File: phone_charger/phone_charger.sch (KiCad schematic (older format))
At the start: 8 parts

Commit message: added in precision enable for phone charger
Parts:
- added R?: 56k (1%), symbol device:R
- added R?: 10.2k (1%), symbol device:R
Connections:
- net labels removed: reg_en
- wire segments 19 -> 24
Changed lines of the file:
@@
 EESchema Schematic File Version 4
+LIBS:phone_charger-cache
 EELAYER 26 0
 EELAYER END
@@
 L device:C C?
 U 1 1 5B8626AF
-P 7500 1500
-F 0 "C?" H 7615 1546 50  0000 L CNN
-F 1 "10u (25V)" H 7615 1455 50  0000 L CNN
-F 2 "" H 7538 1350 50  0001 C CNN
-F 3 "" H 7500 1500 50  0001 C CNN
-	1    7500 1500
+P 7100 1500
+F 0 "C?" H 7215 1546 50  0000 L CNN
+F 1 "10u (25V)" H 7215 1455 50  0000 L CNN
+F 2 "" H 7138 1350 50  0001 C CNN
+F 3 "" H 7100 1500 50  0001 C CNN
+	1    7100 1500
 	1    0    0    -1
 $EndComp
@@
 L power:GND #PWR?
 U 1 1 5B862781
-P 7500 1800
-F 0 "#PWR?" H 7500 1550 50  0001 C CNN
-F 1 "GND" H 7505 1627 50  0000 C CNN
-F 2 "" H 7500 1800 50  0001 C CNN
-F 3 "" H 7500 1800 50  0001 C CNN
-	1    7500 1800
-	1    0    0    -1
-$EndComp
-Wire Wire Line
-	7500 1650 7500 1800
-Wire Wire Line
-	7500 1350 7200 1350
+P 7100 1800
+F 0 "#PWR?" H 7100 1550 50  0001 C CNN
+F 1 "GND" H 7105 1627 50  0000 C CNN
+F 2 "" H 7100 1800 50  0001 C CNN
+F 3 "" H 7100 1800 50  0001 C CNN
+	1    7100 1800
+	1    0    0    -1
+$EndComp
+Wire Wire Line
+	7100 1650 7100 1800
+Wire Wire Line
+	7100 1350 6800 1350
 Wire Wire Line
 	9250 1250 9400 1250
-Text Label 7200 1350 0    50   ~ 0
+Text Label 6800 1350 0    50   ~ 0
 reg_in
 Text Label 10600 1600 0    50   ~ 0
@@
 Wire Wire Line
 	10500 1600 10900 1600
-Wire Wire Line
-	7500 1350 7950 1350
-Connection ~ 7500 1350
-Wire Wire Line
-	7950 1850 7700 1850
-Text Label 7700 1850 0    50   ~ 0
-reg_en
+Connection ~ 7100 1350
 Wire Wire Line
 	10100 1700 10100 1600
@@
 Wire Notes Line
 	6300 500  6300 3350
+$Comp
+L device:R R?
+U 1 1 5B863BCD
+P 7750 1600
+F 0 "R?" H 7820 1646 50  0000 L CNN
+F 1 "56k (1%)" H 7820 1555 50  0000 L CNN
+F 2 "" V 7680 1600 50  0001 C CNN
+F 3 "" H 7750 1600 50  0001 C CNN
+	1    7750 1600
+	1    0    0    -1
+$EndComp
+$Comp
+L device:R R?
+U 1 1 5B863BFA
+P 7750 2100
+F 0 "R?" H 7820 2146 50  0000 L CNN
+F 1 "10.2k (1%)" H 7820 2055 50  0000 L CNN
+F 2 "" V 7680 2100 50  0001 C CNN
+F 3 "" H 7750 2100 50  0001 C CNN
+	1    7750 2100
+	1    0    0    -1
+$EndComp
+$Comp
+L power:GND #PWR?
+U 1 1 5B863C22
+P 7750 2350
+F 0 "#PWR?" H 7750 2100 50  0001 C CNN
+F 1 "GND" H 7755 2177 50  0000 C CNN
+F 2 "" H 7750 2350 50  0001 C CNN
+F 3 "" H 7750 2350 50  0001 C CNN
+	1    7750 2350
+	1    0    0    -1
+$EndComp
+Wire Wire Line
+	7100 1350 7750 1350
+Wire Wire Line
+	7750 1350 7750 1450
+Connection ~ 7750 1350
+Wire Wire Line
+	7750 1350 7950 1350
+Wire Wire Line
+	7750 1750 7750 1850
+Wire Wire Line
+	7750 2250 7750 2350
+Wire Wire Line
+	7750 1850 7950 1850
+Connection ~ 7750 1850
+Wire Wire Line
+	7750 1850 7750 1950
 $EndSCHEMATC

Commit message: Rescue symbols
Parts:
- C? (x3): symbol device:C -> phone_charger-rescue:C-device
- D?: symbol device:D_Schottky -> phone_charger-rescue:D_Schottky-device
- L?: symbol device:L -> phone_charger-rescue:L-device
- R? (x4): symbol device:R -> phone_charger-rescue:R-device
- U?: symbol ADP2301:ADP2301AUJZ-R2 -> phone_charger-rescue:ADP2301AUJZ-R2-ADP2301
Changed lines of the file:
@@
 $EndDescr
 $Comp
-L ADP2301:ADP2301AUJZ-R2 U?
+L phone_charger-rescue:ADP2301AUJZ-R2-ADP2301 U?
 U 1 1 5B85ED45
 P 8600 1600
@@
 $EndComp
 $Comp
-L device:L L?
+L phone_charger-rescue:L-device L?
 U 1 1 5B85F10E
 P 9750 1600
@@
 $EndComp
 $Comp
-L device:C C?
+L phone_charger-rescue:C-device C?
 U 1 1 5B85F280
 P 10500 1850
@@
 $EndComp
 $Comp
-L device:R R?
+L phone_charger-rescue:R-device R?
 U 1 1 5B85F3D3
 P 10100 1850
@@
 $EndComp
 $Comp
-L device:R R?
+L phone_charger-rescue:R-device R?
 U 1 1 5B85F4C9
 P 10100 2300
@@
 $EndComp
 $Comp
-L device:D_Schottky D?
+L phone_charger-rescue:D_Schottky-device D?
 U 1 1 5B861A87
 P 9400 1750
@@
 $EndComp
 $Comp
-L device:C C?
+L phone_charger-rescue:C-device C?
 U 1 1 5B86257D
 P 9400 1400
@@
 $EndComp
 $Comp
-L device:C C?
+L phone_charger-rescue:C-device C?
 U 1 1 5B8626AF
 P 7100 1500
@@
 	6300 500  6300 3350
 $Comp
-L device:R R?
+L phone_charger-rescue:R-device R?
 U 1 1 5B863BCD
 P 7750 1600
@@
 $EndComp
 $Comp
-L device:R R?
+L phone_charger-rescue:R-device R?
 U 1 1 5B863BFA
 P 7750 2100

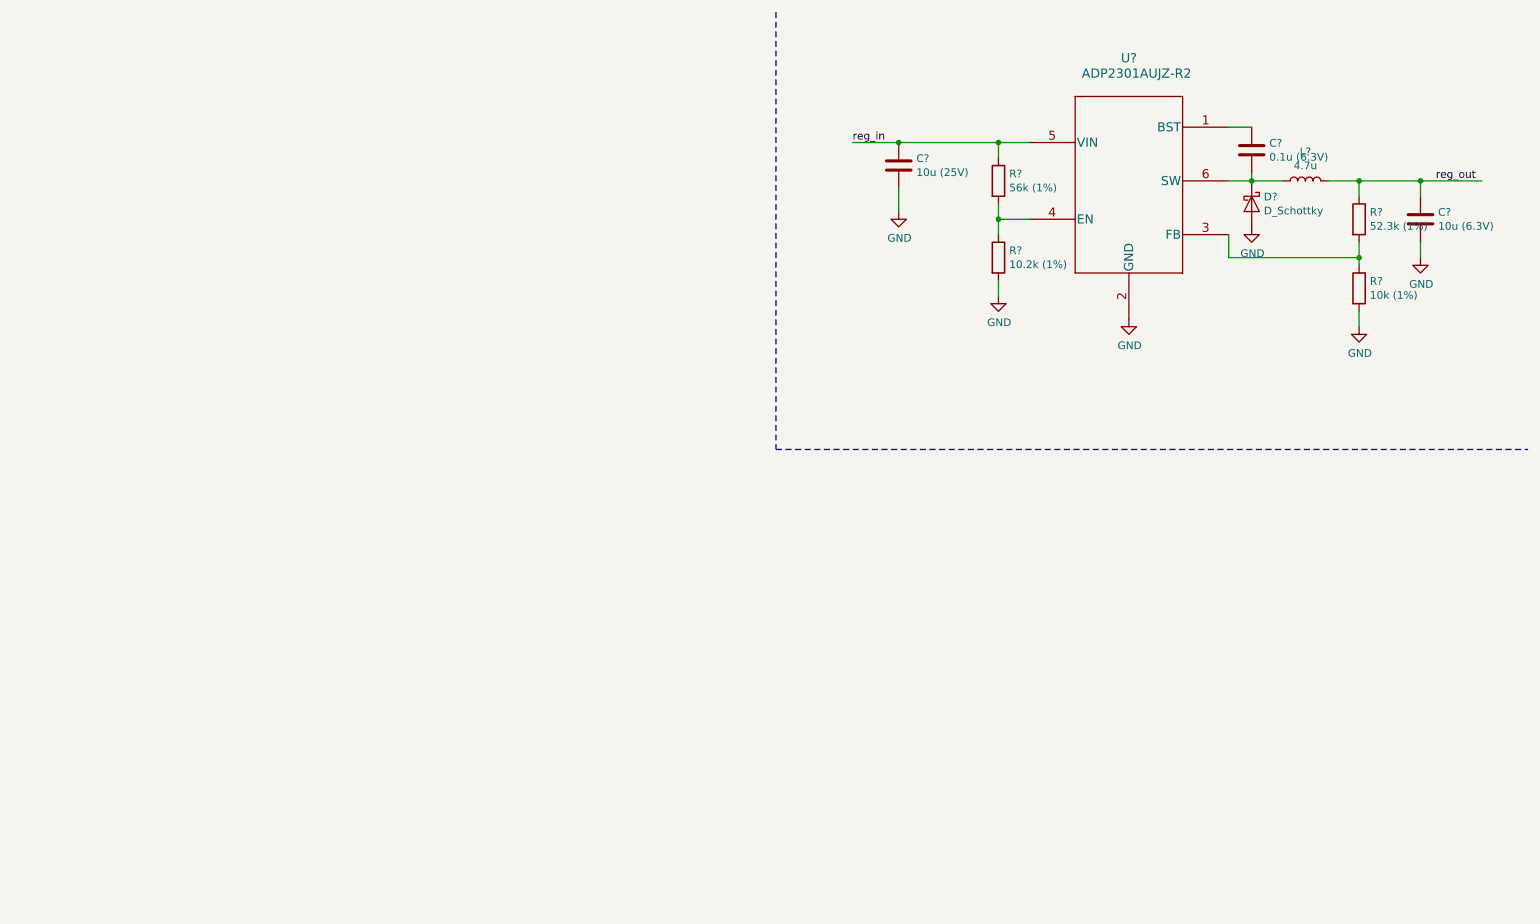
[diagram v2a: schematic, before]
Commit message: Add some top-level details
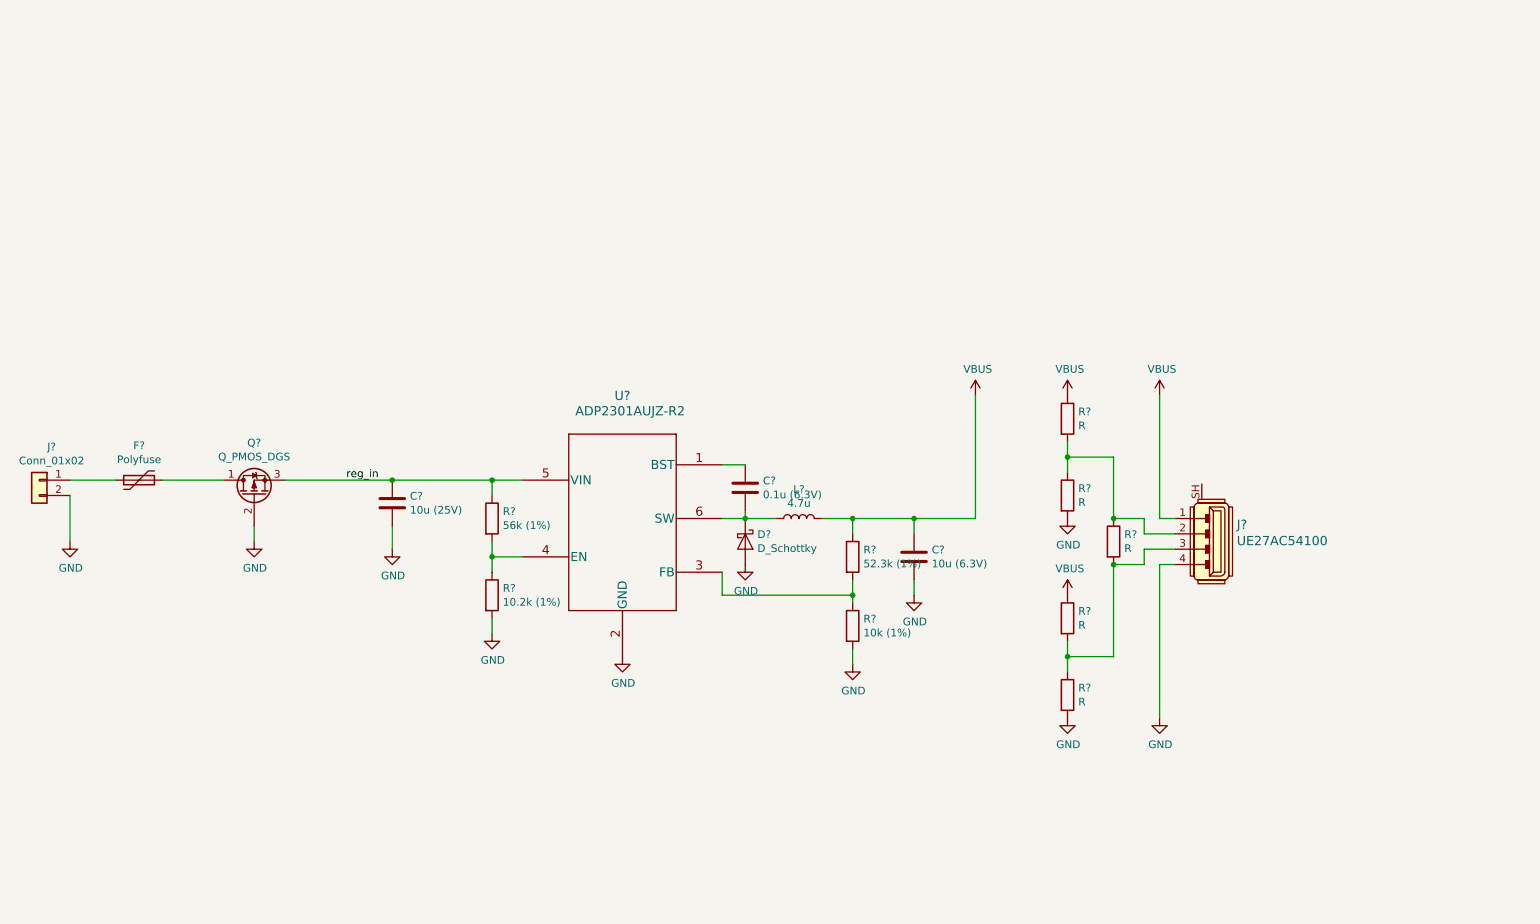
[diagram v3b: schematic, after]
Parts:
- added F?: Polyfuse, symbol Device:Polyfuse
- added J?: UE27AC54100, digikey-footprints:USB_A_Female_UE27AC54100, symbol dk_USB-DVI-HDMI-Connectors:UE27AC54100
- added J?: Conn_01x02, symbol Connector_Generic:Conn_01x02
- added Q?: Q_PMOS_DGS, symbol Device:Q_PMOS_DGS
- added R? (x5): R, symbol Device:R
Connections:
- net labels added: VBUS
- net labels removed: reg_out
- wire segments 24 -> 47
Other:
- moved on the sheet: C?, D?, L?, R?, U?

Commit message: Add values
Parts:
- R?: value R -> 75k
- R? (x2): value R -> 50k
- R?: value R -> 43k
- R?: value R -> 200
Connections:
- net D-: now reaches J?.2, R?.1, R?.1, R?.2
- net D+: now reaches J?.3, R?.1, R?.2, R?.2
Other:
- note added: "Populate EITHER Apple divider resistors or 200 ohm short."
- moved on the sheet: J?
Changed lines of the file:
@@
 L dk_USB-DVI-HDMI-Connectors:UE27AC54100 J?
 U 1 1 5B88DA27
-P 9200 3900
-F 0 "J?" H 9097 3840 60  0000 R CNN
-F 1 "UE27AC54100" H 9097 3946 60  0000 R CNN
-F 2 "digikey-footprints:USB_A_Female_UE27AC54100" H 9400 4100 60  0001 L CNN
-F 3 "https://www.amphenolcanada.com/ProductSearch/drawings/AC/UE27ACX4X0X.pdf" H 9400 4200 60  0001 L CNN
-F 4 "UE27AC54100-ND" H 9400 4300 60  0001 L CNN "Digi-Key_PN"
-F 5 "UE27AC54100" H 9400 4400 60  0001 L CNN "MPN"
-F 6 "Connectors, Interconnects" H 9400 4500 60  0001 L CNN "Category"
-F 7 "USB, DVI, HDMI Connectors" H 9400 4600 60  0001 L CNN "Family"
-F 8 "https://www.amphenolcanada.com/ProductSearch/drawings/AC/UE27ACX4X0X.pdf" H 9400 4700 60  0001 L CNN "DK_Datasheet_Link"
-F 9 "/product-detail/en/amphenol-commercial-products/UE27AC54100/UE27AC54100-ND/1972253" H 9400 4800 60  0001 L CNN "DK_Detail_Page"
-F 10 "CONN RCPT USB TYPE A R/A GOLD" H 9400 4900 60  0001 L CNN "Description"
-F 11 "Amphenol Commercial Products" H 9400 5000 60  0001 L CNN "Manufacturer"
-F 12 "Active" H 9400 5100 60  0001 L CNN "Status"
-	1    9200 3900
+P 9400 3900
+F 0 "J?" H 9297 3840 60  0000 R CNN
+F 1 "UE27AC54100" H 9297 3946 60  0000 R CNN
+F 2 "digikey-footprints:USB_A_Female_UE27AC54100" H 9600 4100 60  0001 L CNN
+F 3 "https://www.amphenolcanada.com/ProductSearch/drawings/AC/UE27ACX4X0X.pdf" H 9600 4200 60  0001 L CNN
+F 4 "UE27AC54100-ND" H 9600 4300 60  0001 L CNN "Digi-Key_PN"
+F 5 "UE27AC54100" H 9600 4400 60  0001 L CNN "MPN"
+F 6 "Connectors, Interconnects" H 9600 4500 60  0001 L CNN "Category"
+F 7 "USB, DVI, HDMI Connectors" H 9600 4600 60  0001 L CNN "Family"
+F 8 "https://www.amphenolcanada.com/ProductSearch/drawings/AC/UE27ACX4X0X.pdf" H 9600 4700 60  0001 L CNN "DK_Datasheet_Link"
+F 9 "/product-detail/en/amphenol-commercial-products/UE27AC54100/UE27AC54100-ND/1972253" H 9600 4800 60  0001 L CNN "DK_Detail_Page"
+F 10 "CONN RCPT USB TYPE A R/A GOLD" H 9600 4900 60  0001 L CNN "Description"
+F 11 "Amphenol Commercial Products" H 9600 5000 60  0001 L CNN "Manufacturer"
+F 12 "Active" H 9600 5100 60  0001 L CNN "Status"
+	1    9400 3900
 	-1   0    0    1
 $EndComp
@@
 P 8200 3150
 F 0 "R?" H 8270 3196 50  0000 L CNN
-F 1 "R" H 8270 3105 50  0000 L CNN
+F 1 "75k" H 8270 3105 50  0000 L CNN
 F 2 "" V 8130 3150 50  0001 C CNN
 F 3 "~" H 8200 3150 50  0001 C CNN
@@
 P 8200 3650
 F 0 "R?" H 8270 3696 50  0000 L CNN
-F 1 "R" H 8270 3605 50  0000 L CNN
+F 1 "50k" H 8270 3605 50  0000 L CNN
 F 2 "" V 8130 3650 50  0001 C CNN
 F 3 "~" H 8200 3650 50  0001 C CNN
@@
 P 8200 4450
 F 0 "R?" H 8270 4496 50  0000 L CNN
-F 1 "R" H 8270 4405 50  0000 L CNN
+F 1 "43k" H 8270 4405 50  0000 L CNN
 F 2 "" V 8130 4450 50  0001 C CNN
 F 3 "~" H 8200 4450 50  0001 C CNN
@@
 P 8200 4950
 F 0 "R?" H 8270 4996 50  0000 L CNN
-F 1 "R" H 8270 4905 50  0000 L CNN
+F 1 "50k" H 8270 4905 50  0000 L CNN
 F 2 "" V 8130 4950 50  0001 C CNN
 F 3 "~" H 8200 4950 50  0001 C CNN
@@
 P 8500 3950
 F 0 "R?" H 8570 3996 50  0000 L CNN
-F 1 "R" H 8570 3905 50  0000 L CNN
+F 1 "200" H 8570 3905 50  0000 L CNN
 F 2 "" V 8430 3950 50  0001 C CNN
 F 3 "~" H 8500 3950 50  0001 C CNN
@@
 $EndComp
 Wire Wire Line
-	8900 3900 8700 3900
-Wire Wire Line
-	8700 3900 8700 3800
-Wire Wire Line
-	8900 4000 8700 4000
-Wire Wire Line
-	8700 4000 8700 4100
-Wire Wire Line
-	8700 4100 8500 4100
-Wire Wire Line
-	8700 3800 8500 3800
-Wire Wire Line
 	8500 3400 8500 3800
 Connection ~ 8500 3800
@@
 L power:GND #PWR?
 U 1 1 5B89256C
-P 8800 5100
-F 0 "#PWR?" H 8800 4850 50  0001 C CNN
-F 1 "GND" H 8805 4927 50  0000 C CNN
-F 2 "" H 8800 5100 50  0001 C CNN
-F 3 "" H 8800 5100 50  0001 C CNN
-	1    8800 5100
-	1    0    0    -1
-$EndComp
-Wire Wire Line
-	8900 4100 8800 4100
-Wire Wire Line
-	8800 4100 8800 5100
+P 9000 5100
+F 0 "#PWR?" H 9000 4850 50  0001 C CNN
+F 1 "GND" H 9005 4927 50  0000 C CNN
+F 2 "" H 9000 5100 50  0001 C CNN
+F 3 "" H 9000 5100 50  0001 C CNN
+	1    9000 5100
+	1    0    0    -1
+$EndComp
+Wire Wire Line
+	9100 4100 9000 4100
+Wire Wire Line
+	9000 4100 9000 5100
 $Comp
 L power:VBUS #PWR?
 U 1 1 5B892D7D
-P 8800 3000
-F 0 "#PWR?" H 8800 2850 50  0001 C CNN
-F 1 "VBUS" H 8815 3173 50  0000 C CNN
-F 2 "" H 8800 3000 50  0001 C CNN
-F 3 "" H 8800 3000 50  0001 C CNN
-	1    8800 3000
-	1    0    0    -1
-$EndComp
-Wire Wire Line
-	8800 3000 8800 3800
-Wire Wire Line
-	8800 3800 8900 3800
+P 9000 3000
+F 0 "#PWR?" H 9000 2850 50  0001 C CNN
+F 1 "VBUS" H 9015 3173 50  0000 C CNN
+F 2 "" H 9000 3000 50  0001 C CNN
+F 3 "" H 9000 3000 50  0001 C CNN
+	1    9000 3000
+	1    0    0    -1
+$EndComp
+Wire Wire Line
+	9000 3000 9000 3800
+Wire Wire Line
+	9000 3800 9100 3800
 $Comp
 L Device:Polyfuse F?
@@
 Wire Wire Line
 	7600 3800 7600 3000
+Text Label 8950 3900 0    50   ~ 0
+D-
+Text Label 8950 4000 0    50   ~ 0
+D+
+Text Notes 7400 5500 0    50   ~ 0
+Populate EITHER Apple divider resistors or 200 ohm short.
+Wire Wire Line
+	8800 3900 8800 3800
+Wire Wire Line
+	8800 3900 9100 3900
+Wire Wire Line
+	8500 3800 8800 3800
+Wire Wire Line
+	8800 4000 8800 4100
+Wire Wire Line
+	8800 4000 9100 4000
+Wire Wire Line
+	8500 4100 8800 4100
 $EndSCHEMATC

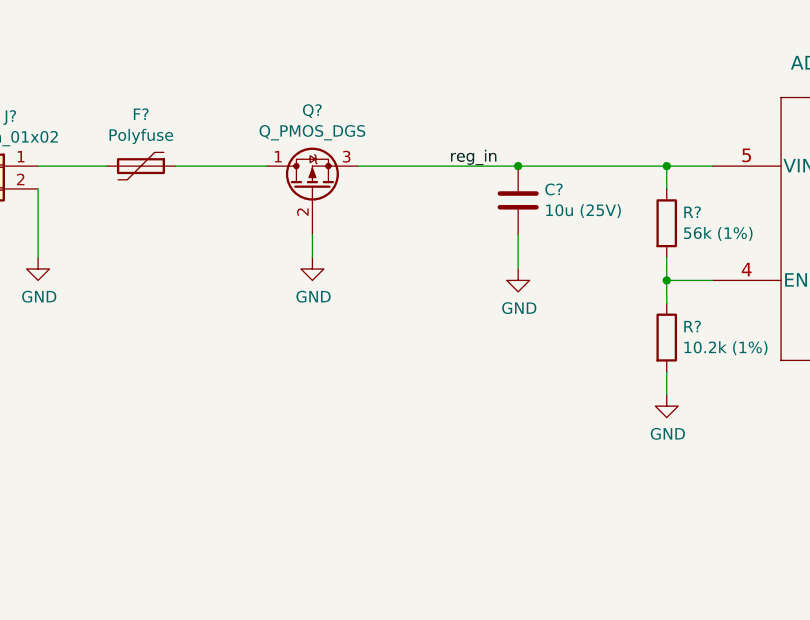
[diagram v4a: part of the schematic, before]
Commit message: Add gate protection
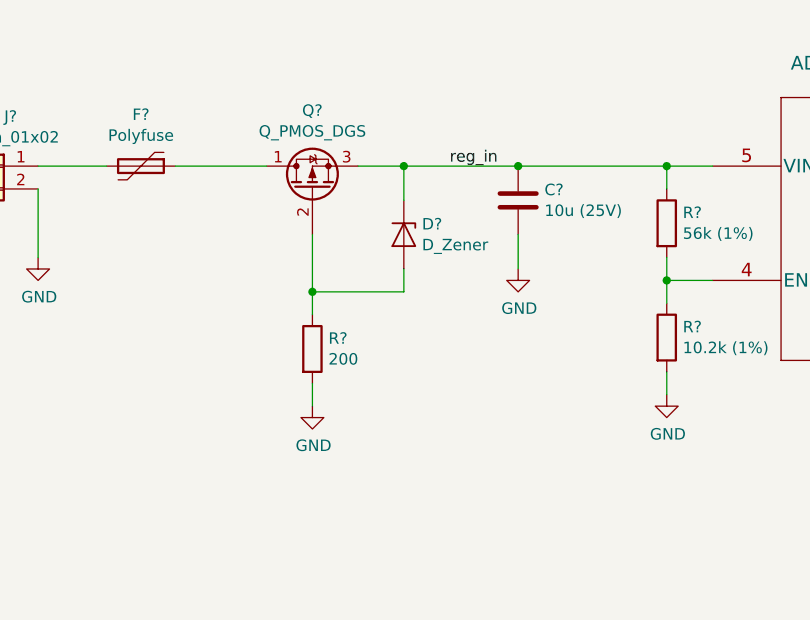
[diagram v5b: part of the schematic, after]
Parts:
- added D?: D_Zener, symbol Device:D_Zener
- added R?: 200, symbol Device:R
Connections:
- net GND: now also R?.2; no longer Q?.2 (G)
- net reg_in: now also D?.1 (K)
- new net: D?.2 (A), Q?.2 (G), R?.1
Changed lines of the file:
@@
 L power:GND #PWR?
 U 1 1 5B897F30
-P 2900 3950
-F 0 "#PWR?" H 2900 3700 50  0001 C CNN
-F 1 "GND" H 2905 3777 50  0000 C CNN
-F 2 "" H 2900 3950 50  0001 C CNN
-F 3 "" H 2900 3950 50  0001 C CNN
-	1    2900 3950
+P 2900 4600
+F 0 "#PWR?" H 2900 4350 50  0001 C CNN
+F 1 "GND" H 2905 4427 50  0000 C CNN
+F 2 "" H 2900 4600 50  0001 C CNN
+F 3 "" H 2900 4600 50  0001 C CNN
+	1    2900 4600
 	1    0    0    -1
 $EndComp
-Wire Wire Line
-	2900 3850 2900 3950
 Connection ~ 3800 3550
 Wire Wire Line
-	3100 3550 3800 3550
+	3100 3550 3300 3550
 Wire Wire Line
 	7600 3800 7600 3000
@@
 Wire Wire Line
 	8500 4100 8800 4100
+$Comp
+L Device:D_Zener D?
+U 1 1 5B8A2F34
+P 3300 3850
+F 0 "D?" V 3254 3929 50  0000 L CNN
+F 1 "D_Zener" V 3345 3929 50  0000 L CNN
+F 2 "" H 3300 3850 50  0001 C CNN
+F 3 "~" H 3300 3850 50  0001 C CNN
+	1    3300 3850
+	0    1    1    0
+$EndComp
+Wire Wire Line
+	3300 3700 3300 3550
+Connection ~ 3300 3550
+Wire Wire Line
+	3300 3550 3800 3550
+Wire Wire Line
+	2900 3850 2900 4100
+Wire Wire Line
+	3300 4100 3300 4000
+$Comp
+L Device:R R?
+U 1 1 5B8A6F51
+P 2900 4350
+F 0 "R?" H 2970 4396 50  0000 L CNN
+F 1 "200" H 2970 4305 50  0000 L CNN
+F 2 "" V 2830 4350 50  0001 C CNN
+F 3 "~" H 2900 4350 50  0001 C CNN
+	1    2900 4350
+	1    0    0    -1
+$EndComp
+Wire Wire Line
+	2900 4600 2900 4500
+Wire Wire Line
+	2900 4100 3300 4100
+Wire Wire Line
+	2900 4200 2900 4100
+Connection ~ 2900 4100
 $EndSCHEMATC

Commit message: Phone charger symbol and schematic changes
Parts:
- removed D?: D_Zener, symbol Device:D_Zener
- removed Q?: Q_PMOS_DGS, symbol Device:Q_PMOS_DGS
- removed R?: 52.3k (1%), symbol phone_charger-rescue:R-device
- removed R?: 10k (1%), symbol phone_charger-rescue:R-device
- removed R?: 56k (1%), symbol phone_charger-rescue:R-device
- removed R?: 200, symbol Device:R
- removed U?: ADP2301AUJZ-R2, UJ_6, symbol phone_charger-rescue:ADP2301AUJZ-R2-ADP2301
- added C3: 22u (16V), symbol phone_charger-rescue:C-device
- added D1: LED, symbol Device:LED
- added D2: D_Schottky, symbol Device:D_Schottky
- added R1: R, symbol Device:R
- added U1: ADP2302, UJ_6, symbol phone_charger-rescue:ADP2302
- C4: renamed from C?; value 10u (6.3V) -> 22u (16V)
- D3: renamed from D?; value D_Schottky -> B330B
- F1: renamed from F?; symbol Device:Polyfuse -> phone_charger-rescue:Polyfuse-Device
- J1: renamed from J?; symbol Connector_Generic:Conn_01x02 -> phone_charger-rescue:Conn_01x02-Connector_Generic
- J2: renamed from J?; symbol dk_USB-DVI-HDMI-Connectors:UE27AC54100 -> phone_charger-rescue:UE27AC54100-dk_USB-DVI-HDMI-Connectors
- L1: renamed from L?; value 4.7u -> 6.8u
- R2: renamed from R?; value 10.2k (1%) -> 100k
- R3, R4, R5, R6: renamed from R?; symbol Device:R -> phone_charger-rescue:R-Device
- R7: renamed from R?; value 200 -> 0R (OPT); symbol Device:R -> phone_charger-rescue:R-Device
- gave numbers to parts that had none: 2
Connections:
- wire segments 53 -> 47
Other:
- moved on the sheet: C1, C2, C4, D3, F1, J1, J2, L1, R2, R3, R4, R5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
